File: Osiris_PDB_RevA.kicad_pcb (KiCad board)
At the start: 2 copper layers, 126 x 83.2 mm, 69 parts, among them J1 Phoenix 1932588 125A PROVISIO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, J2 OSIRIS_I2C, J3 Phoenix 1932588 125A PROVISIO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, J4 XT60PW-F, Q1 ISC015N06NM5LF2, Q2 ISC015N06NM5LF2, Q3 BSC070N10NS5, U1 LTC4368HMS-1-PBF, U2 INA228AIDGSR, U3 LT3010EMS8E, U4 74AUP1G07GW, U5 LTC4359IMS8

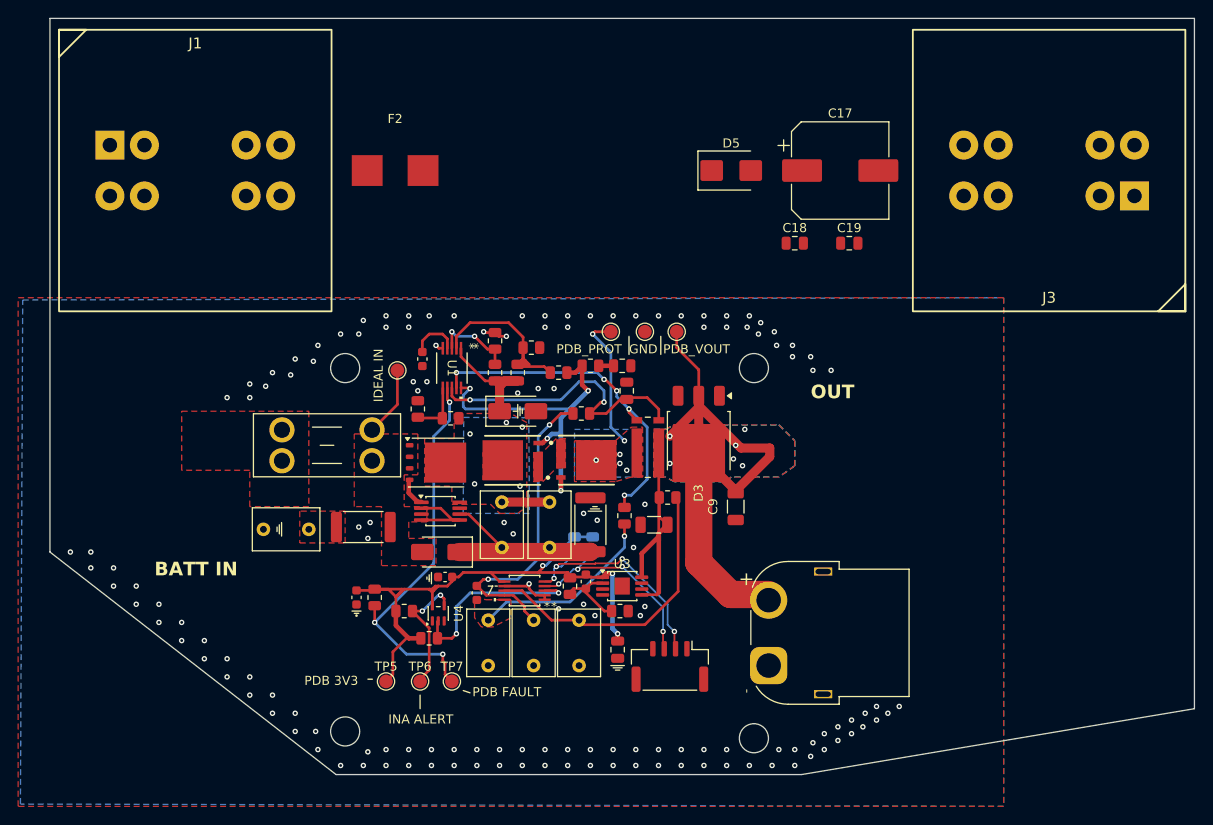
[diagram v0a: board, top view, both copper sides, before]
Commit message: Route compact three-XT60 PDB candidate
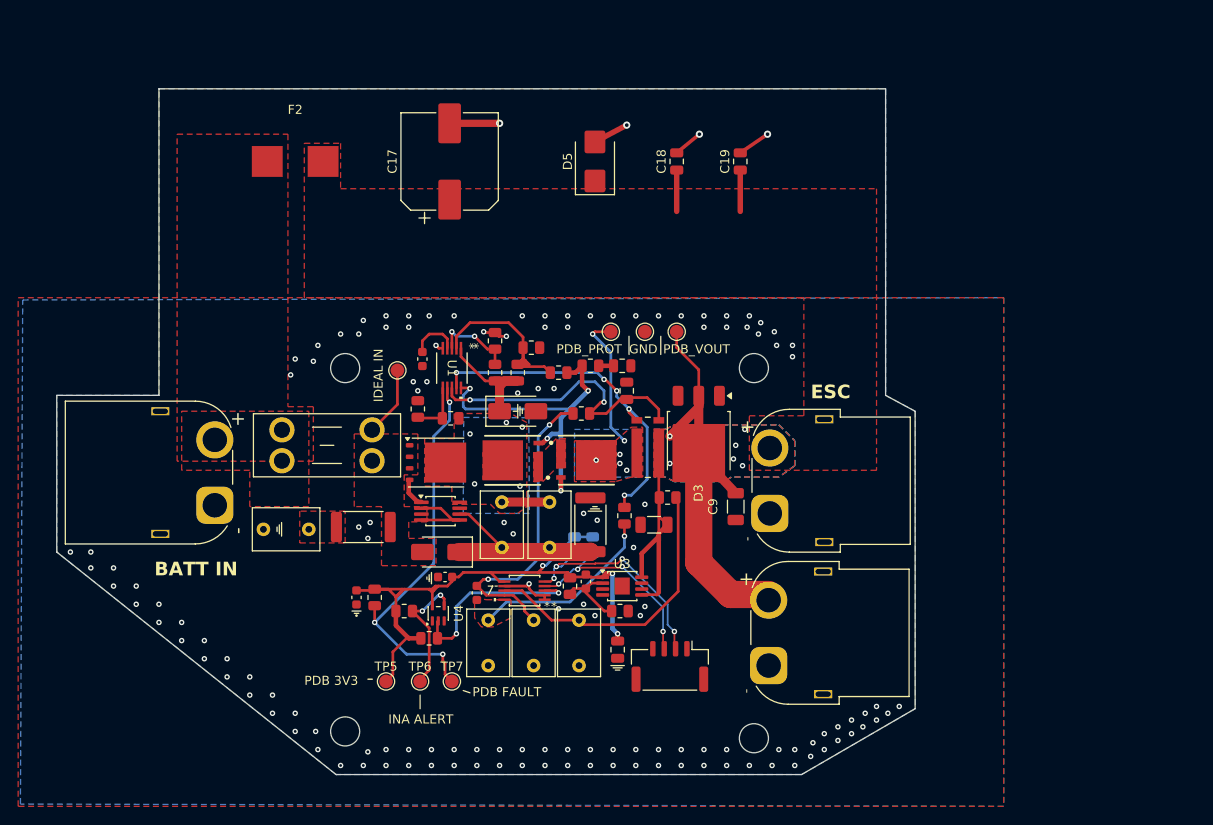
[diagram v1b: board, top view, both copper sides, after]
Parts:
- C17: value 470u 35V LOW-ESR -> 470u/35V; footprint CP_Elec_10x10.5 -> Capacitor_SMD:CP_Elec_10x10.5
- C18: value 1u 50V X7R -> 1u/50V; footprint C_0805_2012Metric -> Capacitor_SMD:C_0805_2012Metric
- C19: value 100n 50V X7R -> 100n/50V; footprint C_0805_2012Metric -> Capacitor_SMD:C_0805_2012Metric
- D5: footprint D_SMB -> Diode_SMD:D_SMB
- F2: value SCHURTER UHS 100A 3-140-177 PROVISIONAL -> UHS 100A; footprint SCHURTER_UHS_8.4x9.4mm_PROVISIONAL -> PDB_Footprints:SCHURTER_UHS_8.4x9.4mm_PROVISIONAL
- J1: value Phoenix 1932588 125A PROVISIONAL -> XT60PW-M; footprint MKDSP25_2_15mm_PROVISIONAL -> Connector_AMASS:AMASS_XT60PW-M_1x02_P7.20mm_Horizontal
- J3: value Phoenix 1932588 125A PROVISIONAL -> XT60PW-F; footprint MKDSP25_2_15mm_PROVISIONAL -> Connector_AMASS:AMASS_XT60PW-F_1x02_P7.20mm_Horizontal
- moved J3 48.7 mm to (92.2, 34.8), turned to -90 degrees
- moved C17 43.0 mm to (57.0, -4.00), turned to 90 degrees
- moved J1 36.9 mm to (31.1, 33.9), turned to 90 degrees
- moved C18 15.8 mm to (82.0, -4.00), turned to 90 degrees
- moved D5 15.0 mm to (73.0, -4.00), turned to 90 degrees
- moved C19 15.0 mm to (89.0, -4.00), turned to 90 degrees
- moved F2 11.0 mm to (40.0, -4.00)
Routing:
- net GND: track 9.46 -> 25.8 mm, vias 144 -> 140
- net /PDB_VOUT: track 92.4 -> 76.6 mm
- net /ESC_VBAT: track 0.00 -> 9.10 mm
- added copper zone on F.Cu, net /ESC_VBAT
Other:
- board size 126 x 83.2 mm -> 94.5 x 75.5 mm
- board text added: "ESC"
- board text removed: "OUT"

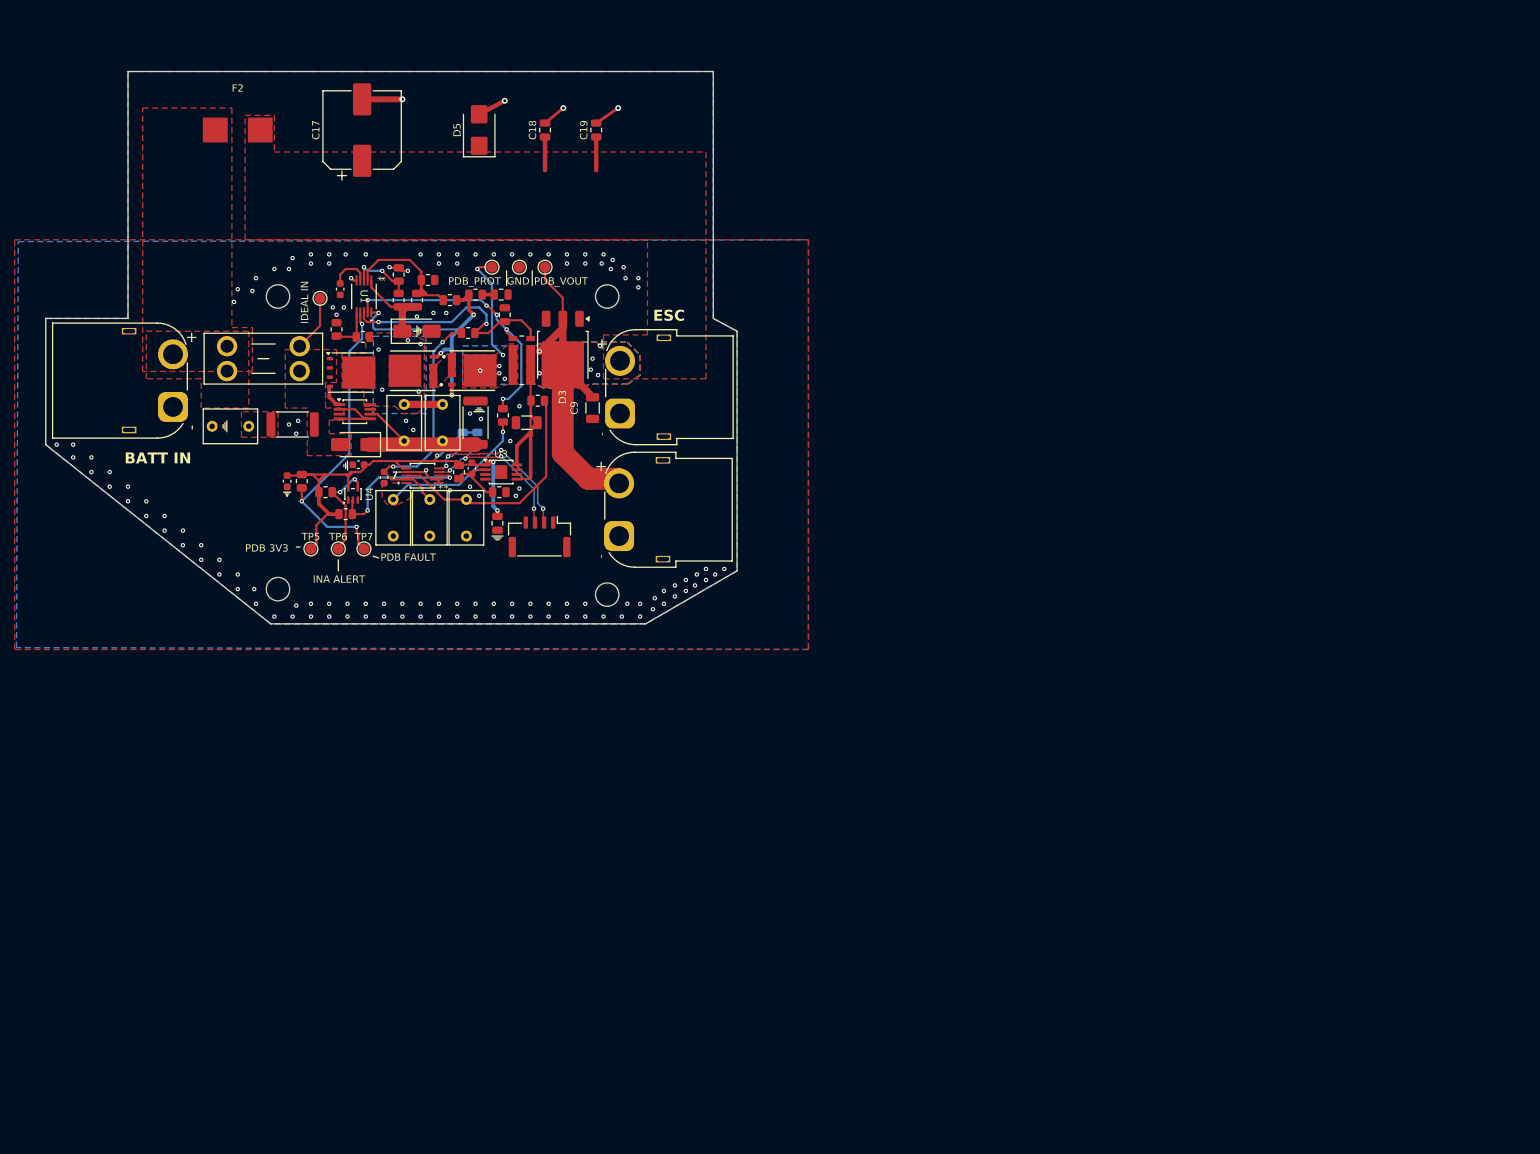
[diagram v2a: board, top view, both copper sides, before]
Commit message: Restore compact PDB layout shown in reference image
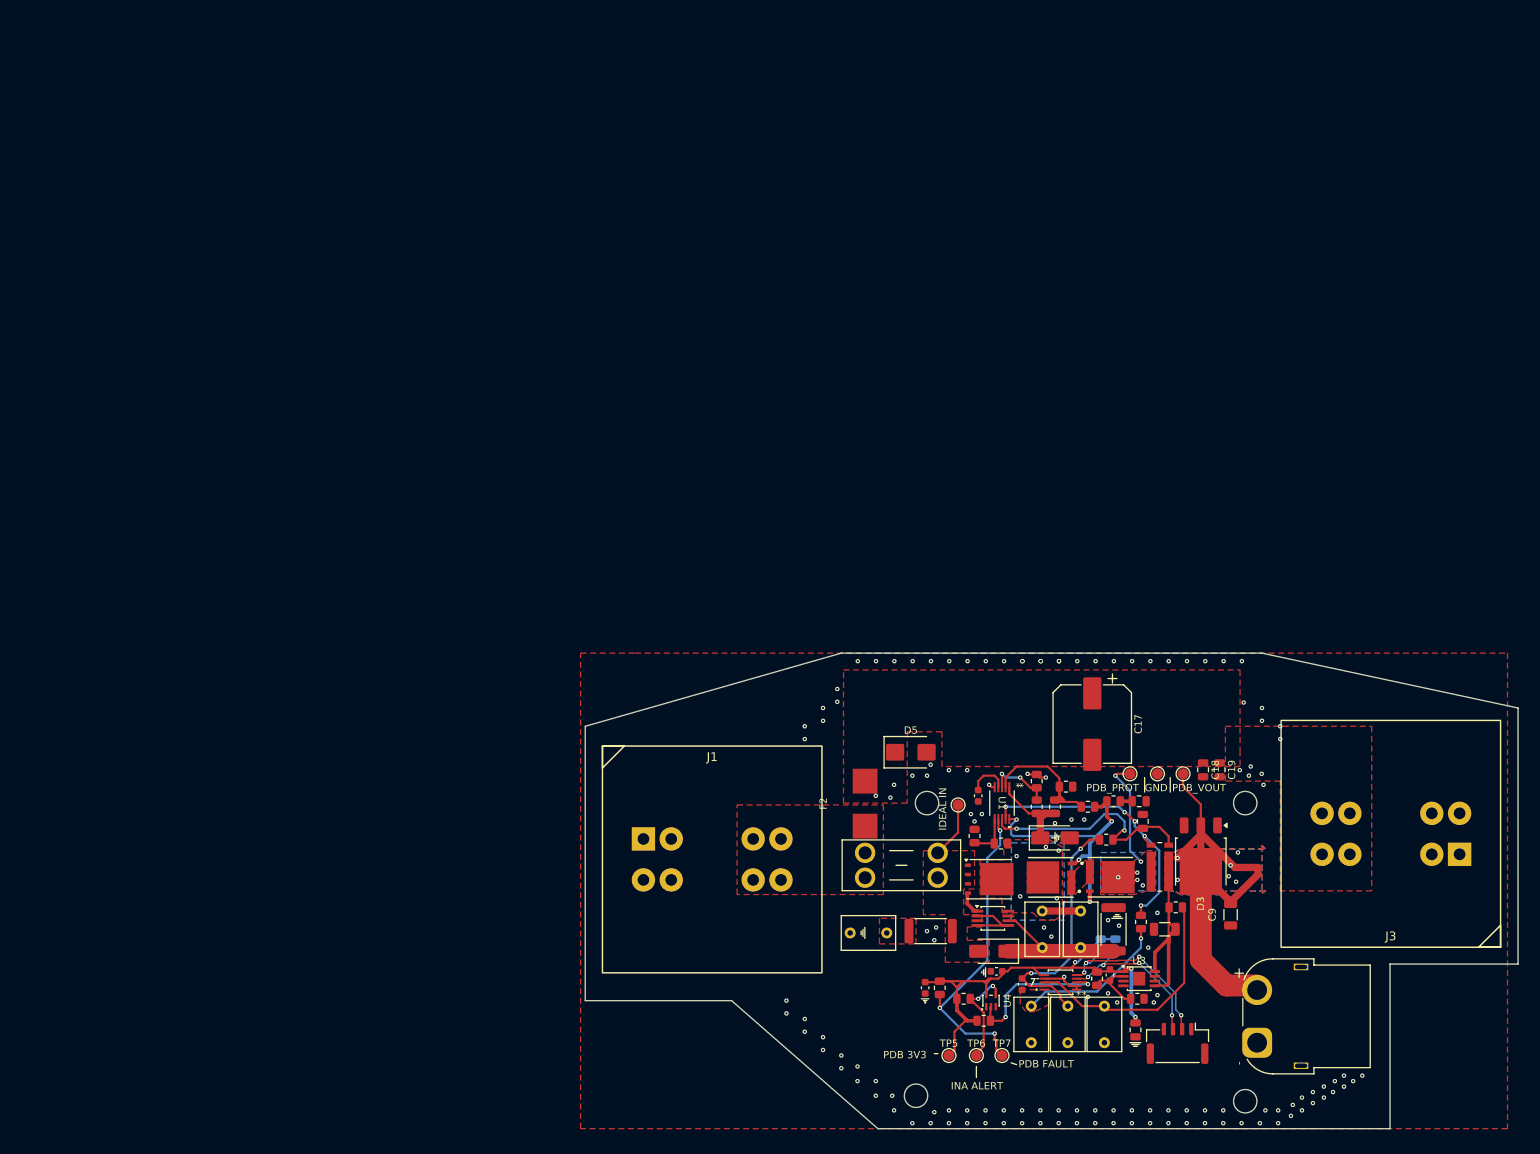
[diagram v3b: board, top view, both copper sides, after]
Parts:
- C17: value 470u/35V -> 470u 35V LOW-ESR
- C18: value 1u/50V -> 1u 50V X7R
- C19: value 100n/50V -> 100n 50V X7R
- F2: value UHS 100A -> SCHURTER UHS 100A 3-140-177 PROVISIONAL
- J1: value XT60PW-M -> MKDSP 25/2-15.00 PROVISIONAL; footprint Connector_AMASS:AMASS_XT60PW-M_1x02_P7.20mm_Horizontal -> PDB_Footprints:MKDSP25_2_15mm_PROVISIONAL
- J3: value XT60PW-F -> MKDSP 25/2-15.00 PROVISIONAL; footprint Connector_AMASS:AMASS_XT60PW-F_1x02_P7.20mm_Horizontal -> PDB_Footprints:MKDSP25_2_15mm_PROVISIONAL
- moved C17 128.7 mm to (156.8, 77.2), turned to -90 degrees
- moved F2 125.8 mm to (125.8, 88.1), turned to 90 degrees
- moved C18 125.5 mm to (171.9, 83.5), turned to -90 degrees
- moved C19 122.1 mm to (174.2, 83.5), turned to -90 degrees
- moved J3 120.0 mm to (197.6, 92.2), turned to 180 degrees
- moved H1 112.5 mm to (134.2, 88.0)
- moved C1 111.4 mm to (163.2, 87.8)
- moved C10 111.4 mm to (159.2, 111.5)
- moved C11 111.4 mm to (150.0, 102.8)
- moved C12 111.4 mm to (148.5, 115.8)
- moved C13 111.4 mm to (153.5, 115.8)
- moved C14 111.4 mm to (158.5, 115.8)
- moved C15 111.4 mm to (155.2, 102.8)
- moved C16 111.4 mm to (128.7, 105.8)
- moved C2 111.4 mm to (163.7, 90.5)
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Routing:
- net GND: track 25.8 -> 9.46 mm, vias 140 -> 141
- net /PDB_VOUT: track 76.6 -> 92.4 mm
- net /ESC_VBAT: track 9.10 -> 0.00 mm
- removed copper zone on B.Cu, net GND
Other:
- board size 94.5 x 75.5 mm -> 127.5 x 65 mm
- board text removed: "BATT IN"
- board text removed: "ESC"

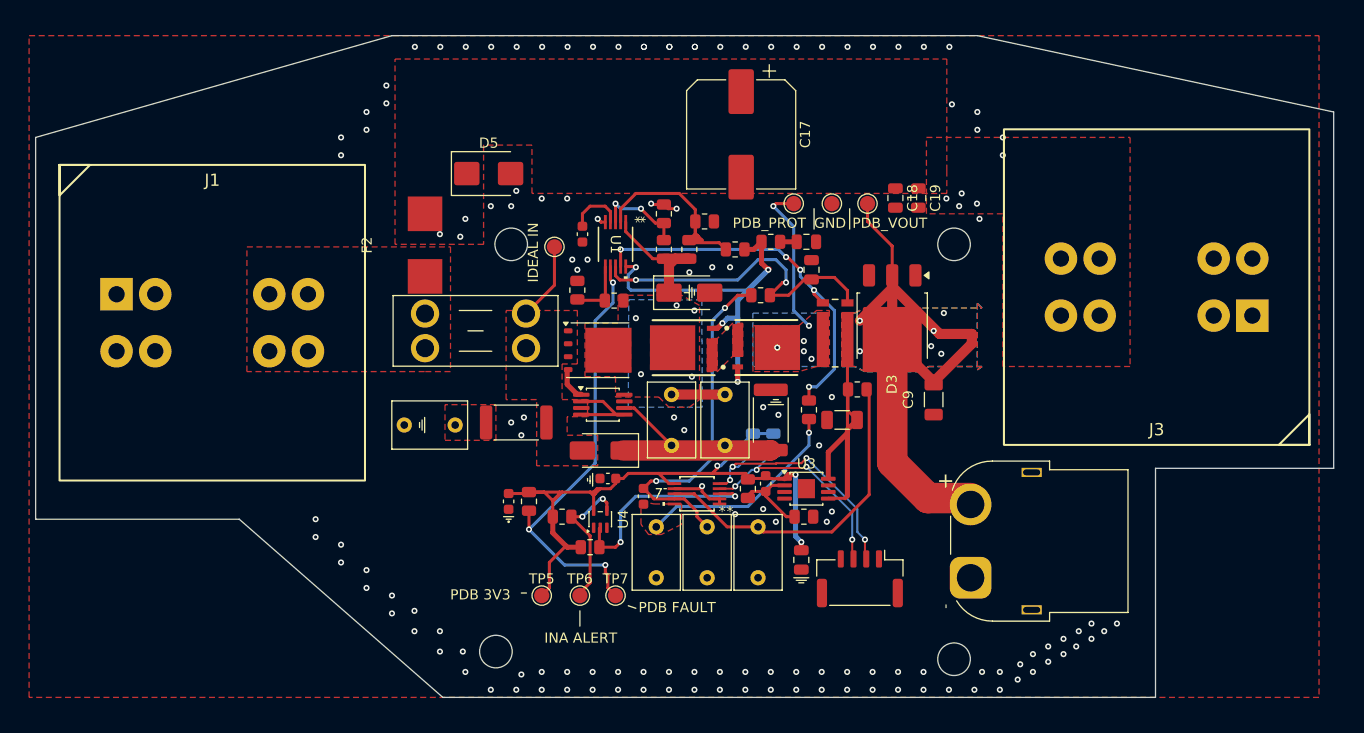
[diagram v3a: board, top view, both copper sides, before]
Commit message: Update PDB design and purchasing deliverables
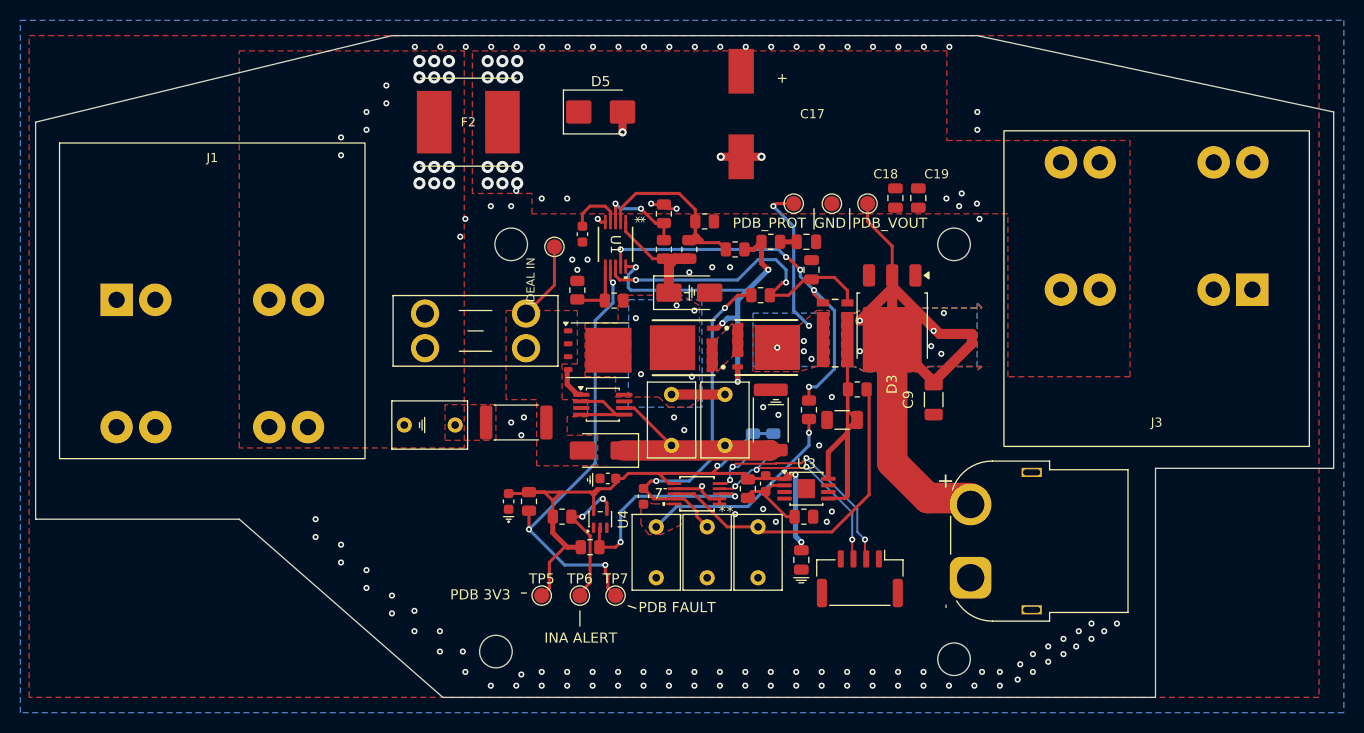
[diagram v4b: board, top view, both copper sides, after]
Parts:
- C17: value 470u 35V LOW-ESR -> 470u 35V HYBRID; footprint Capacitor_SMD:CP_Elec_10x10.5 -> PDB_Footprints:CP_Elec_Panasonic_G16_10x16.5
- F2: value SCHURTER UHS 100A 3-140-177 PROVISIONAL -> UHS 100A 50V; footprint PDB_Footprints:SCHURTER_UHS_8.4x9.4mm_PROVISIONAL -> PDB_Footprints:Fuse_SCHURTER_UHS_8.4x9.4mm
- J1, J3: value MKDSP 25/2-15.00 PROVISIONAL -> MKDSP 25/2-15.00; footprint PDB_Footprints:MKDSP25_2_15mm_PROVISIONAL -> PDB_Footprints:Connector_MKDSP25_2_15mm
- moved F2 12.8 mm to (130.0, 76.0), turned to 0 degrees
- moved D5 12.6 mm to (143.0, 75.0)
- moved J3 6.00 mm to (197.6, 86.2)
- moved J1 4.00 mm to (104.8, 99.7)
- moved C17 2.00 mm to (156.8, 75.2)
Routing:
- net GND: track 9.46 -> 15.5 mm, vias 141 -> 138
- net /VBAT_RAW: vias 0 -> 12
- net /ESC_VBAT: vias 0 -> 11
- added copper zone on In2.Cu, net /ESC_VBAT
- added copper zone on In2.Cu, net /VBAT_RAW
- added copper zone on B.Cu, net GND
- added copper zone on In1.Cu, net GND
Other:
- outline, holes or cut-outs redrawn
- copper layers 2 -> 4

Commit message: fixed grnd fault
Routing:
- net GND: vias 138 -> 137
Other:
- board text removed: "IDEAL IN"
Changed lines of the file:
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@@
 		(layer "Edge.Cuts")
-	)
-	(gr_text "IDEAL IN"
-		(at 136.6 94 90)
-		(layer "F.SilkS")
-		(effects
-			(font
-				(size 0.8 0.8)
-				(thickness 0.1)
-			)
-			(justify left bottom)
-		)
 	)
 	(gr_text "PDB 3V3"
@@
 		(size 0.6)
 		(drill 0.3)
-		(layers "F.Cu" "B.Cu")
-		(free yes)
-		(net "GND")
-	)
-	(via
-		(at 157.25 68.6)
-		(size 0.6)
-		(drill 0.3)
